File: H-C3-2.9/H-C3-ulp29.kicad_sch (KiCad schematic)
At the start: 54 parts, among them CN1 HX JN1.27-2X5 TP H4.9, J1 USB_C_Receptacle_USB2.0, J2 AFC24-S24FIC-00, J4 SM04B-SRSS-TB_LF__SN_, Q1 Si1308, Q2 Si2301CDS, SW1 K2-1806SQ-A2DW-04, SW2 K2-1806SQ-A2DW-04, SW3 K2-1806SQ-A2DW-04, U1 E73-2G4M08S1C, U2 MCP1700-3302E_SOT23, U8 PCF8563T, Y1 Crystal_Small

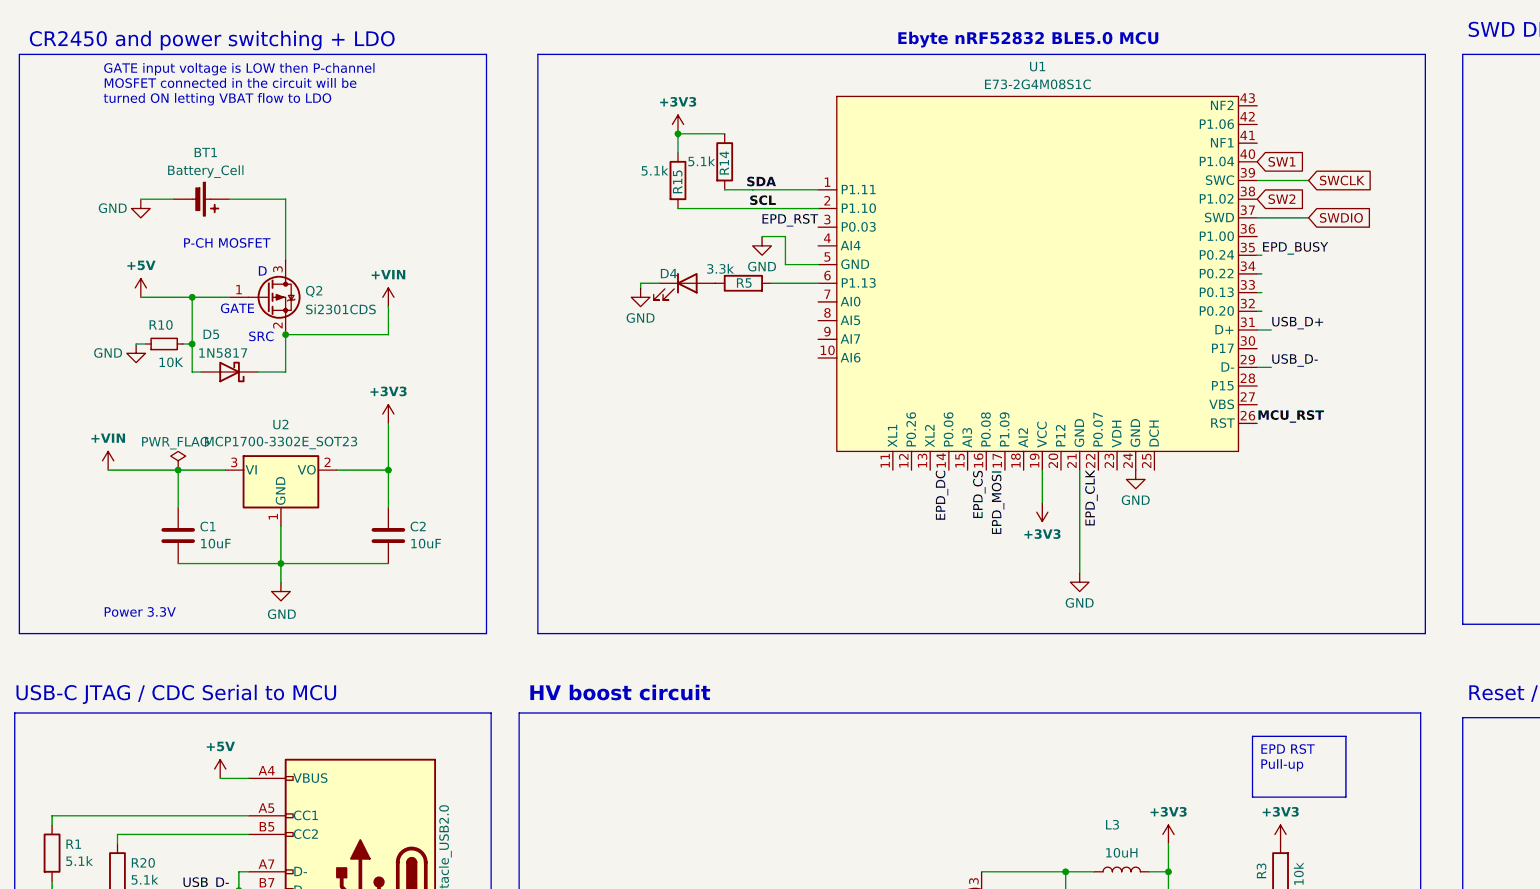
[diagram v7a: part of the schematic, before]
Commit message: Add nRF52 RTC crystal
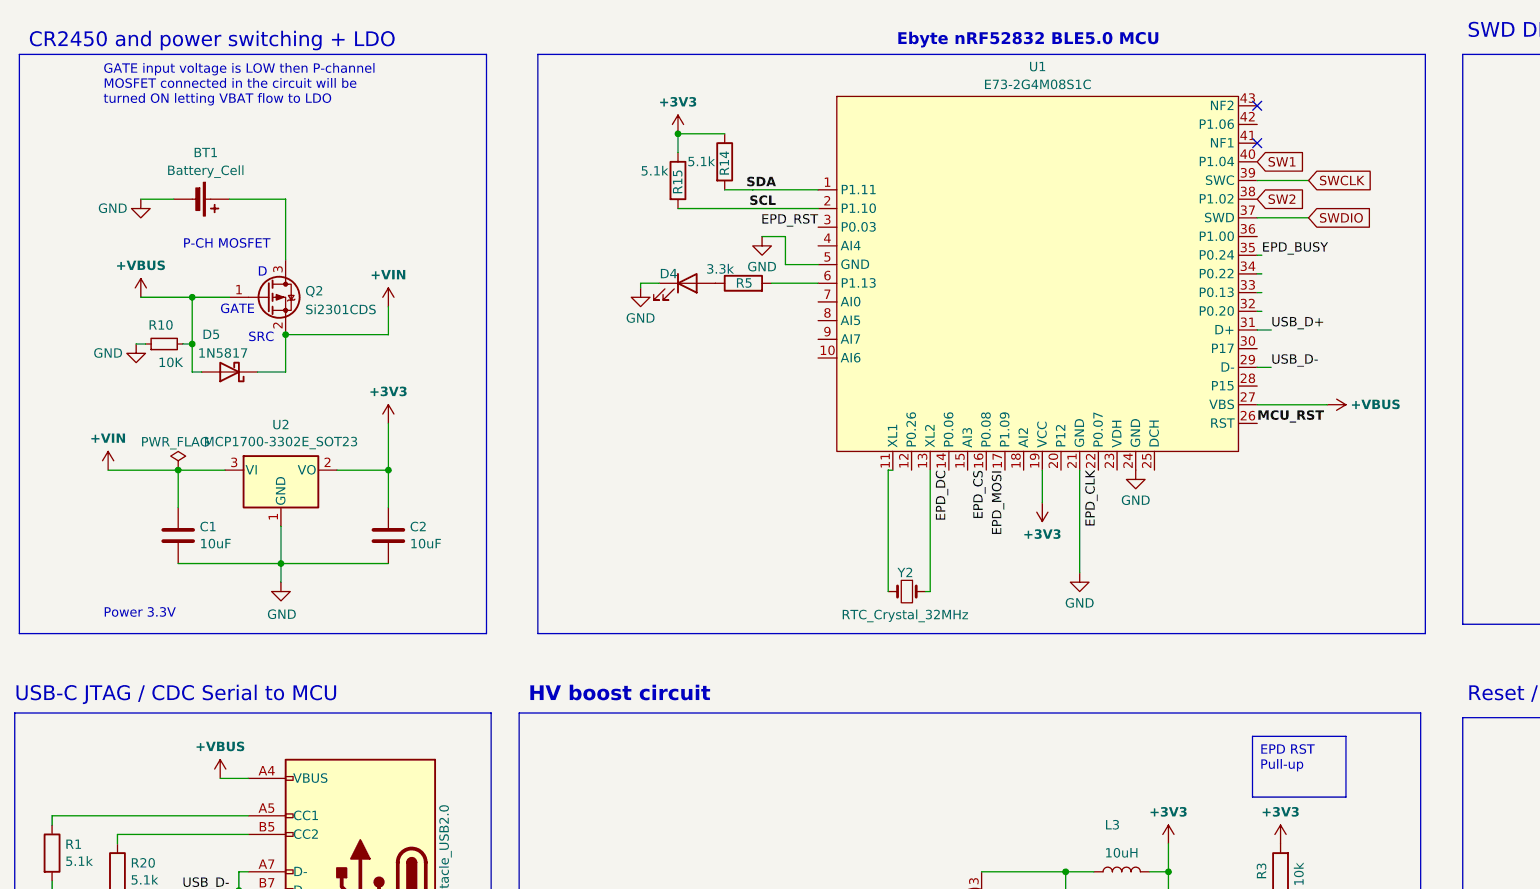
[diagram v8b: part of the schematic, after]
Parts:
- added Y2: RTC_Crystal_32MHz, footprints:Q13FC1350000400-Crystal, symbol Device:Crystal_Small
- BT1: LCSC (none) -> C964809
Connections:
- net +5V is gone; now on net +VBUS: D5.2 (A), J1.A4 (VBUS), J1.A9 (VBUS), J1.B4 (VBUS), J1.B9 (VBUS), Q2.1 (G), R10.2
- net at U1.11 (XL1): now also Y2.2
- net at U1.13 (XL2): now also Y2.1
- net +VBUS: now reaches U1.27 (VBS)
- no-connect marks 10 -> 12
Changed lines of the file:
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@@
 	)
 	(no_connect
+		(at 190.5 52.07)
+	)
+	(no_connect
 		(at 128.905 186.69)
 	)
 	(no_connect
+		(at 190.5 46.99)
+	)
+	(no_connect
 		(at 274.32 154.94)
 	)
@@
 	(wire
 		(pts
+			(xy 146.05 96.52) (xy 146.05 113.03)
+		)
+		(stroke
+			(width 0)
+			(type default)
+		)
+	)
+	(wire
+		(pts
 			(xy 226.695 173.99) (xy 230.505 173.99)
 		)
@@
 	(wire
 		(pts
+			(xy 200.025 87.63) (xy 190.5 87.63)
+		)
+		(stroke
+			(width 0)
+			(type default)
+		)
+	)
+	(wire
+		(pts
 			(xy 111.76 50.8) (xy 118.11 50.8)
 		)
@@
 	(wire
 		(pts
+			(xy 146.05 113.03) (xy 145.415 113.03)
+		)
+		(stroke
+			(width 0)
+			(type default)
+		)
+	)
+	(wire
+		(pts
 			(xy 178.435 151.13) (xy 178.435 153.67)
 		)
@@
 	(wire
 		(pts
+			(xy 140.97 96.52) (xy 140.335 96.52)
+		)
+		(stroke
+			(width 0)
+			(type default)
+		)
+	)
+	(wire
+		(pts
 			(xy 163.195 176.53) (xy 160.655 176.53)
 		)
@@
 	(wire
 		(pts
+			(xy 140.335 96.52) (xy 140.335 113.03)
+		)
+		(stroke
+			(width 0)
+			(type default)
+		)
+	)
+	(wire
+		(pts
 			(xy 128.905 231.14) (xy 128.905 238.76)
 		)
@@
 	)
 	(symbol
-		(lib_id "power:+3V3")
-		(at 38.735 73.025 0)
-		(unit 1)
-		(exclude_from_sim no)
-		(in_bom yes)
-		(on_board yes)
-		(dnp no)
-		(fields_autoplaced yes)
-		(property "Reference" "#PWR10"
-			(at 38.735 76.835 0)
-			(effects
-				(font
-					(size 1.27 1.27)
-				)
-				(hide yes)
-			)
-		)
-		(property "Value" "+5V"
-			(at 38.735 68.7248 0)
-			(effects
-				(font
-					(size 1.27 1.27)
-					(thickness 0.254)
-					(bold yes)
-				)
-			)
-		)
-		(property "Footprint" ""
-			(at 38.735 73.025 0)
-			(effects
-				(font
-					(size 1.27 1.27)
-				)
-				(hide yes)
-			)
-		)
-		(property "Datasheet" ""
-			(at 38.735 73.025 0)
-			(effects
-				(font
-					(size 1.27 1.27)
-				)
-				(hide yes)
-			)
-		)
-		(property "Description" "Power symbol creates a global label with name \"+3V3\""
-			(at 38.735 73.025 0)
-			(effects
-				(font
-					(size 1.27 1.27)
-				)
-				(hide yes)
-			)
-		)
-		(pin "1"
-		)
-		(instances
-			(project "H-C3-ulp29"
-				(path "/4820ae53-5724-49d2-a676-459cc31081bd"
-					(reference "#PWR10")
-					(unit 1)
-				)
-			)
-		)
-	)
-	(symbol
 		(lib_id "Device:C")
 		(at 150.495 219.71 270)
@@
 			)
 		)
-		(property "Value" "+5V"
+		(property "Value" "+VBUS"
 			(at 49.53 134.1298 0)
 			(effects
@@
 	)
 	(symbol
+		(lib_id "power:+3V3")
+		(at 200.025 87.63 270)
+		(unit 1)
+		(exclude_from_sim no)
+		(in_bom yes)
+		(on_board yes)
+		(dnp no)
+		(fields_autoplaced yes)
+		(property "Reference" "#PWR35"
+			(at 196.215 87.63 0)
+			(effects
+				(font
+					(size 1.27 1.27)
+				)
+				(hide yes)
+			)
+		)
+		(property "Value" "+VBUS"
+			(at 203.2 87.63 90)
+			(effects
+				(font
+					(size 1.27 1.27)
+					(thickness 0.254)
+					(bold yes)
+				)
+				(justify left)
+			)
+		)
+		(property "Footprint" ""
+			(at 200.025 87.63 0)
+			(effects
+				(font
+					(size 1.27 1.27)
+				)
+				(hide yes)
+			)
+		)
+		(property "Datasheet" ""
+			(at 200.025 87.63 0)
+			(effects
+				(font
+					(size 1.27 1.27)
+				)
+				(hide yes)
+			)
+		)
+		(property "Description" "Power symbol creates a global label with name \"+3V3\""
+			(at 200.025 87.63 0)
+			(effects
+				(font
+					(size 1.27 1.27)
+				)
+				(hide yes)
+			)
+		)
+		(pin "1"
+		)
+		(instances
+			(project "H-C3-ulp29"
+				(path "/4820ae53-5724-49d2-a676-459cc31081bd"
+					(reference "#PWR35")
+					(unit 1)
+				)
+			)
+		)
+	)
+	(symbol
 		(lib_id "power:GND")
 		(at 132.715 184.15 0)
@@
 			)
 		)
+		(property "LCSC" "C964809"
+			(at 45.72 59.69 90)
+			(effects
+				(font
+					(size 1.27 1.27)
+				)
+				(hide yes)
+			)
+		)
 		(pin "2"
 		)
@@
 	)
 	(symbol
+		(lib_id "power:+3V3")
+		(at 38.735 73.025 0)
+		(unit 1)
+		(exclude_from_sim no)
+		(in_bom yes)
+		(on_board yes)
+		(dnp no)
+		(fields_autoplaced yes)
+		(property "Reference" "#PWR10"
+			(at 38.735 76.835 0)
+			(effects
+				(font
+					(size 1.27 1.27)
+				)
+				(hide yes)
+			)
+		)
+		(property "Value" "+VBUS"
+			(at 38.735 68.7248 0)
+			(effects
+				(font
+					(size 1.27 1.27)
+					(thickness 0.254)
+					(bold yes)
+				)
+			)
+		)
+		(property "Footprint" ""
+			(at 38.735 73.025 0)
+			(effects
+				(font
+					(size 1.27 1.27)
+				)
+				(hide yes)
+			)
+		)
+		(property "Datasheet" ""
+			(at 38.735 73.025 0)
+			(effects
+				(font
+					(size 1.27 1.27)
+				)
+				(hide yes)
+			)
+		)
+		(property "Description" "Power symbol creates a global label with name \"+3V3\""
+			(at 38.735 73.025 0)
+			(effects
+				(font
+					(size 1.27 1.27)
+				)
+				(hide yes)
+			)
+		)
+		(pin "1"
+		)
+		(instances
+			(project "H-C3-ulp29"
+				(path "/4820ae53-5724-49d2-a676-459cc31081bd"
+					(reference "#PWR10")
+					(unit 1)
+				)
+			)
+		)
+	)
+	(symbol
 		(lib_id "power:GND")
 		(at 68.58 179.07 0)
@@
 					(unit 1)
 				)
+			)
+		)
+	)
+	(symbol
+		(lib_id "Device:Crystal_Small")
+		(at 142.875 113.03 180)
+		(unit 1)
+		(exclude_from_sim no)
+		(in_bom yes)
+		(on_board yes)
+		(dnp no)
+		(property "Reference" "Y2"
+			(at 141.605 110.49 0)
+			(effects
+				(font
+					(size 1.27 1.27)
+				)
+				(justify right)
+			)
+		)
+		(property "Value" "RTC_Crystal_32MHz"
+			(at 133.985 116.205 0)
+			(effects
+				(font
+					(size 1.27 1.27)
+				)
+				(justify right)
+			)
+		)
+		(property "Footprint" "footprints:Q13FC1350000400-Crystal"
+			(at 142.875 113.03 0)
+			(effects
+				(font
+					(size 1.27 1.27)
+				)
+				(hide yes)
+			)
+		)
+		(property "Datasheet" "https://jlcpcb.com/partdetail/SeikoEpson-Q13FC1350000400/C32346"
+			(at 142.875 113.03 0)
+			(effects
+				(font
+					(size 1.27 1.27)
+				)
+				(hide yes)
+			)
+		)
+		(property "Description" ""
+			(at 142.875 113.03 0)
+			(effects
+				(font
+					(size 1.27 1.27)
+				)
+				(hide yes)
+			)
+		)
+		(property "LCSC" "C32346"
+			(at 142.875 113.03 90)
+			(effects
+				(font
+					(size 1.27 1.27)
+				)
+				(hide yes)
+			)
+		)
+		(pin "1"
+		)
+		(pin "2"
+		)
+		(instances
+			(project "H-C3-ulp29"
+				(path "/4820ae53-5724-49d2-a676-459cc31081bd"
+					(reference "Y2")
+					(unit 1)
+				)
